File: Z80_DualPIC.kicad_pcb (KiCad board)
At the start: 2 copper layers, 39 parts, among them J1 ICSP, J2 UART, J3 I2C, J4 microSD, J5 DE15_Socket_HighDensity_Mount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, J6 M1_O, J7 USB_B_Mini, J8 Free_Pins, SW1 Slider_Switch, SW2 Z80_RESET, U1 Z84C00_PLCC, U2 PIC1-MMU, U3 AS6C4008-55PCN, U6 PIC2-IO-PROG, Y1 CXO_DIP8, Y2 Crystal

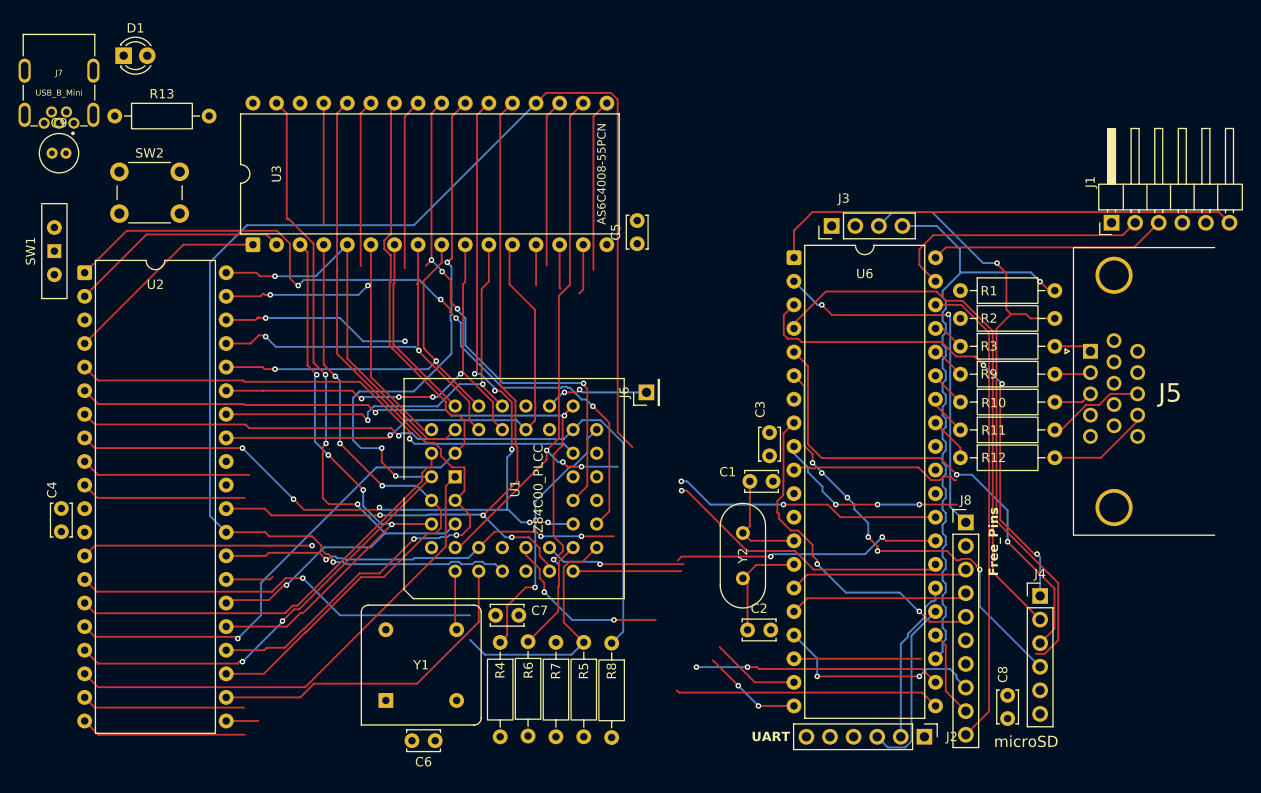
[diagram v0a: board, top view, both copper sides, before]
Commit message: finish routing & added README.md
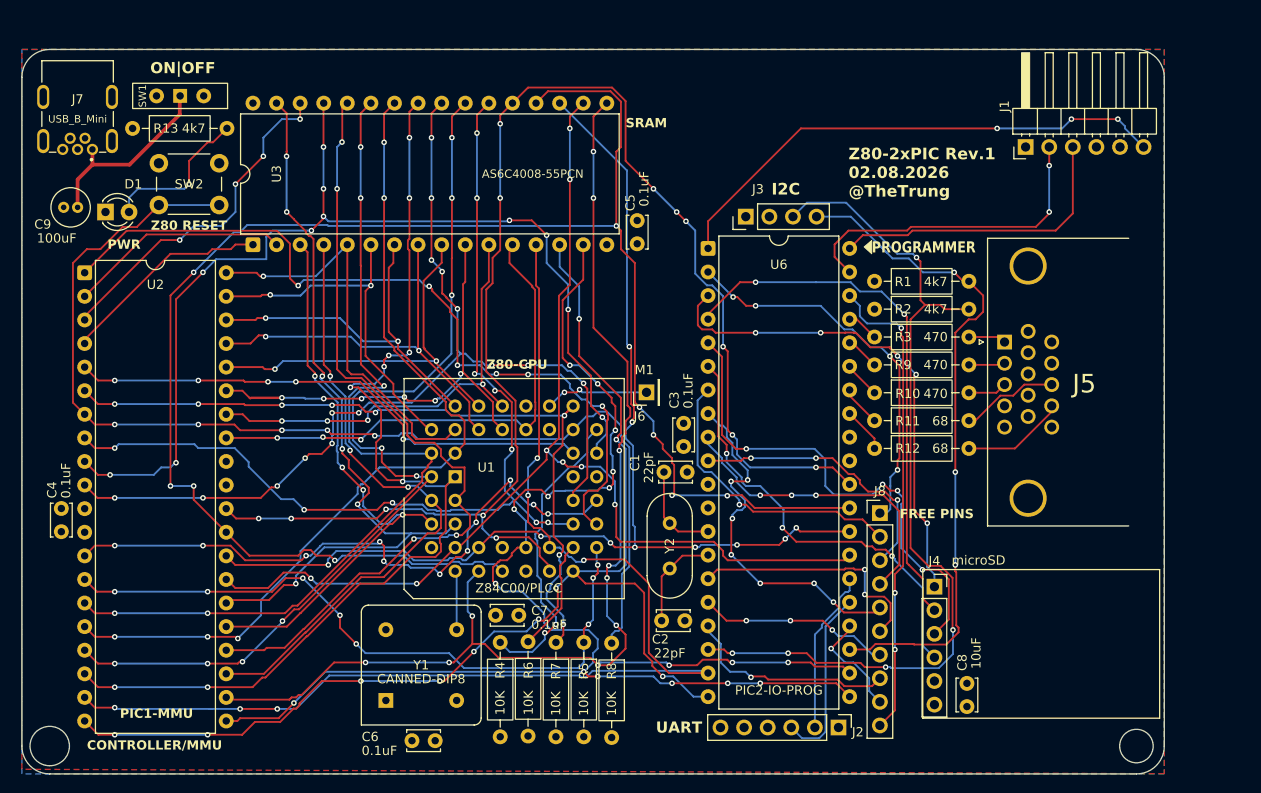
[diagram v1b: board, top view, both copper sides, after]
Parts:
- D1: value LED-PWR -> PWR
- J4: footprint Connector_PinHeader_2.54mm:PinHeader_1x06_P2.54mm_Vertical -> Connector_PinSocket_2.54mm:PinSocket_1x06_P2.54mm_Vertical
- J5: value DE15_Socket_HighDensity_MountingHoles -> VGA-DB15
- J6: value M1_O -> M1
- J8: value Free_Pins -> FREE PINS
- SW1: value Slider_Switch -> ON|OFF
- SW2: value Z80_RESET -> Z80 RESET
- U1: value Z84C00_PLCC -> Z84C00/PLCC
- Y1: value CXO_DIP8 -> CANNED-DIP8
- moved SW1 21.5 mm to (154.5, 35.0), turned to 180 degrees
- moved D1 16.9 mm to (146.5, 47.5)
- moved J1 12.3 mm to (245.6, 40.5)
- moved J4 11.4 mm to (235.8, 87.8)
- moved C1 9.30 mm to (206.6, 75.5)
- moved C2 9.30 mm to (206.4, 91.5)
- moved C3 9.30 mm to (208.8, 72.8)
- moved J2 9.30 mm to (225.4, 103.0)
- moved J3 9.30 mm to (215.4, 48.0)
- moved J5 9.30 mm to (243.3, 61.5)
- moved J8 9.30 mm to (229.9, 79.9)
- moved R1 9.30 mm to (229.3, 55.0)
- moved R10 9.30 mm to (229.3, 67.0)
- moved R11 9.30 mm to (229.3, 70.0)
- moved R12 9.30 mm to (229.3, 73.0)
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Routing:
- net /D2: track 56.3 -> 142.5 mm, vias 2 -> 14
- net /D0: track 46.8 -> 131.8 mm, vias 1 -> 6
- net /D1: track 45.1 -> 130.1 mm, vias 2 -> 10
- net /WR: track 31.3 -> 113.4 mm, vias 0 -> 11
- net /D7: track 85.9 -> 159.1 mm, vias 3 -> 13
- net /D3: track 81.0 -> 147.4 mm, vias 2 -> 13
- net /IORQ: track 24.9 -> 68.0 mm, vias 1 -> 11
- net /A11: track 72.1 -> 110.6 mm, vias 0 -> 9
- net /RESET: track 83.2 -> 120.8 mm, vias 1 -> 5
- net /A17: track 0.00 -> 37.0 mm, vias 0 -> 4
- net /D5: track 90.9 -> 124.2 mm, vias 5 -> 10
- net /A8: track 64.3 -> 96.7 mm, vias 0 -> 5
- net /RD: track 74.5 -> 106.2 mm, vias 4 -> 15
- net /RA5: track 0.00 -> 31.7 mm, vias 0 -> 1
- net /D4: track 98.4 -> 123.1 mm, vias 4 -> 8
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- added copper zone on B.Cu, net GND
- added copper zone on F.Cu, net VCC
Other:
- board outline added: 123 x 78 mm
- board text added: "CONTROLLER/MMU"
- board text added: "PROGRAMMER"
- board text added: "SRAM"
- board text added: "Z80-2xPIC Rev.1 02.08.2026 @TheTrung"
- board text added: "Z80-CPU"

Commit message: add IORQ, WR, RD & A0~A6 into PIC#2
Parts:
- removed C3: 0.1uF, Capacitor_THT:C_Disc_D3.4mm_W2.1mm_P2.50mm
- removed J8: FREE PINS, Connector_PinHeader_2.54mm:PinHeader_1x10_P2.54mm_Vertical
- SW2: value Z80 RESET -> Z80_RESET
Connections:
- U6 pad 10: /RE2 -> /MOSI
- U6 pad 15: /RC0 -> /VSYNC
- U6 pad 16: /RC1 -> /HSYNC
- U6 pad 17: /RC2 -> /SCK
- U6 pad 2: /RA0 -> /A0
- U6 pad 24: /RC5 -> /CS
- U6 pad 3: /CS -> /A1
- U6 pad 33: /VSYNC -> /IORQ
- U6 pad 34: /HSYNC -> /RD
- U6 pad 35: /BLUE -> /WR
- U6 pad 36: /GREEN -> /BLUE
- U6 pad 37: /RED -> /GREEN
- U6 pad 38: /RB5 -> /RED
- U6 pad 4: /SCK -> /A2
- U6 pad 5: /MOSI -> /A3
- U6 pad 6: /MISO -> /A4
- U6 pad 7: /RA5 -> /A5
- U6 pad 8: /RE0 -> /A6
- U6 pad 9: /RE1 -> /MISO
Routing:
- net /RB5: track 51.6 -> 0.00 mm, vias 3 -> 0
- net /A6: track 39.8 -> 87.2 mm, vias 2 -> 5
- net /A5: track 40.2 -> 83.6 mm, vias 2 -> 6
- net /CS: track 54.6 -> 11.3 mm, vias 5 -> 0
- net /RA0: track 41.9 -> 0.00 mm, vias 4 -> 0
- net /RE0: track 39.2 -> 0.00 mm, vias 7 -> 0
- net /A4: track 44.5 -> 83.6 mm, vias 2 -> 6
- net /HSYNC: track 4.41 -> 40.0 mm
- net /IORQ: track 68.0 -> 103.5 mm, vias 11 -> 16
- net /A3: track 43.9 -> 78.2 mm, vias 2 -> 6
- net /RE1: track 33.6 -> 0.00 mm, vias 3 -> 0
- net /RA5: track 31.7 -> 0.00 mm, vias 1 -> 0
- net /WR: track 113.4 -> 145.0 mm, vias 11 -> 14
- net /VSYNC: track 4.87 -> 35.4 mm
- net /RD: track 106.2 -> 136.5 mm, vias 15 -> 17
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
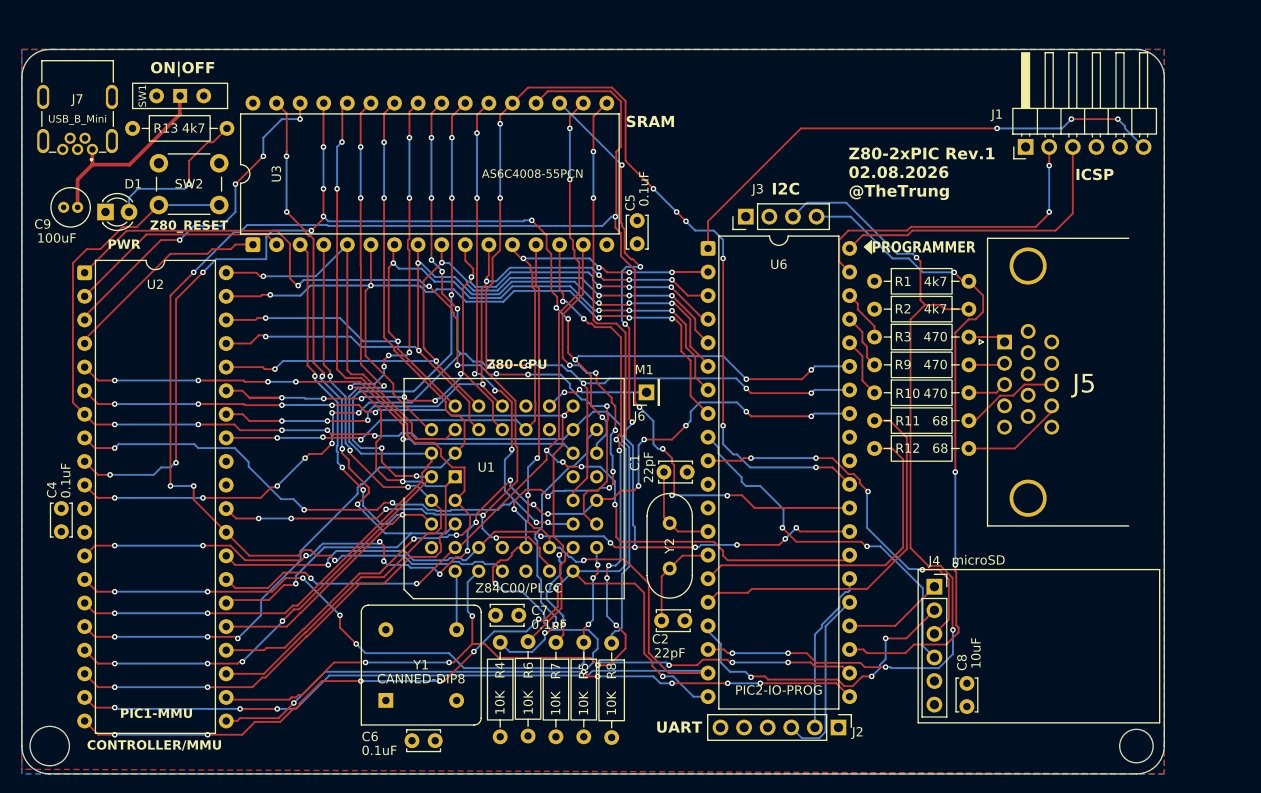
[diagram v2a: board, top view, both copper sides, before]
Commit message: Refine routes + microSD placement.
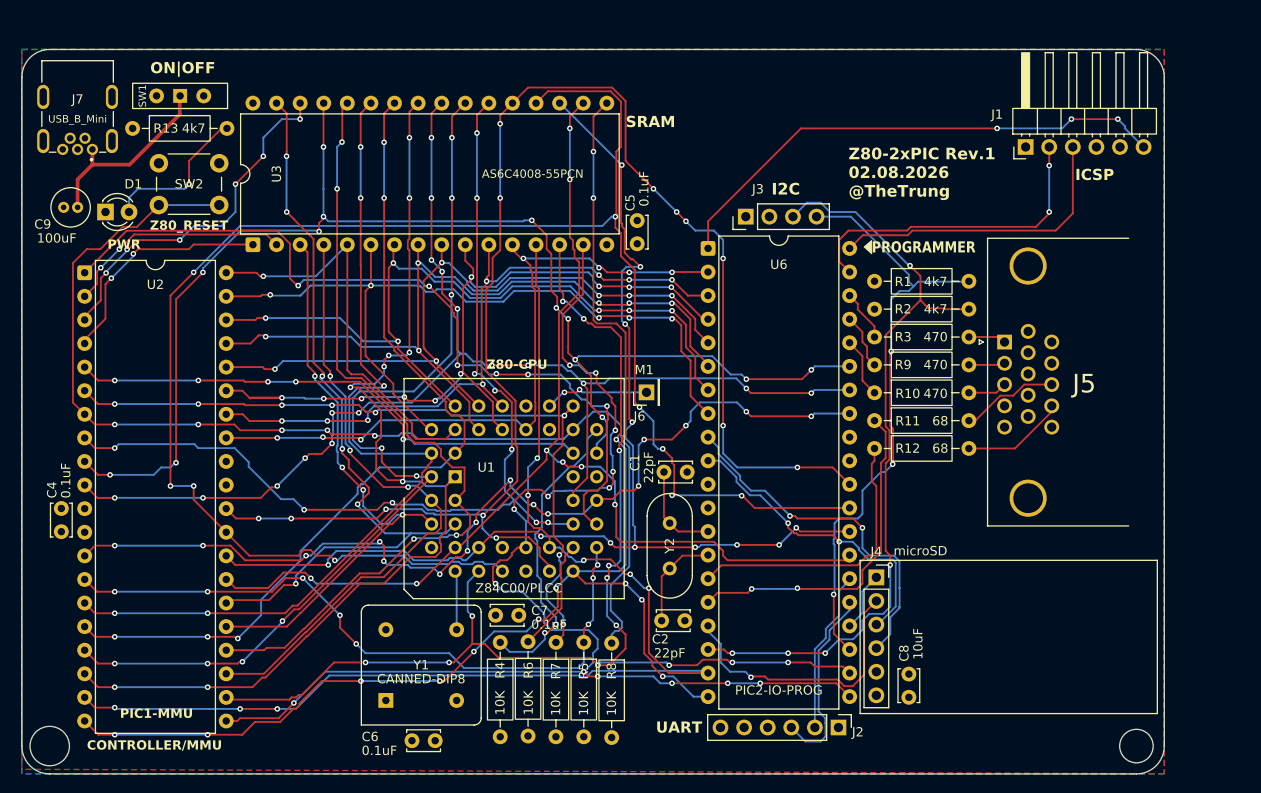
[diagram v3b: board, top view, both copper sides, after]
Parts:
- moved C8 6.33 mm to (233.0, 99.8)
- moved J4 6.33 mm to (229.5, 86.8)
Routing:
- net /SCL: track 95.6 -> 83.4 mm
- net /MOSI: track 40.6 -> 33.0 mm, vias 4 -> 2
- net /SDA: track 74.1 -> 66.6 mm
- net /VSYNC: track 35.4 -> 30.7 mm
- net /CS: track 11.3 -> 6.86 mm
- net /SCK: track 33.5 -> 30.1 mm, vias 3 -> 1
- net /HSYNC: track 40.0 -> 36.6 mm, vias 0 -> 2
- net /A18: track 22.8 -> 25.1 mm, vias 0 -> 2
- net /A17: track 37.0 -> 38.6 mm, vias 4 -> 6
- net /MISO: track 39.9 -> 38.5 mm
- net /TX: track 19.5 -> 20.7 mm
- net /RESET: track 120.8 -> 121.8 mm
- net /A16: track 23.9 -> 24.7 mm, vias 0 -> 2
- net /D1: track 131.5 -> 130.9 mm, vias 11 -> 13
- net /D7: track 160.1 -> 160.7 mm
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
